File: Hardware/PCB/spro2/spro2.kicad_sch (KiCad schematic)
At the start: 7 parts

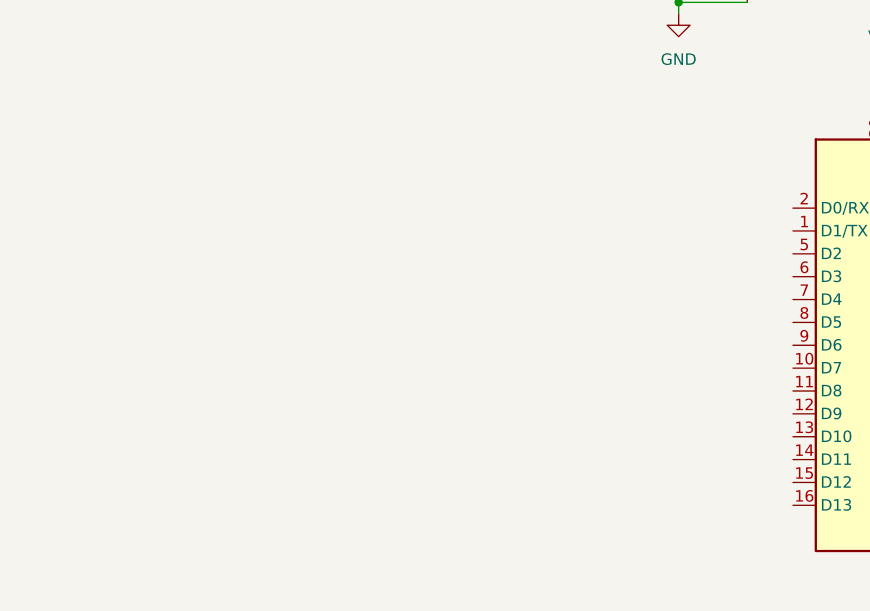
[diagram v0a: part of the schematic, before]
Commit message: Added the temperature schematics
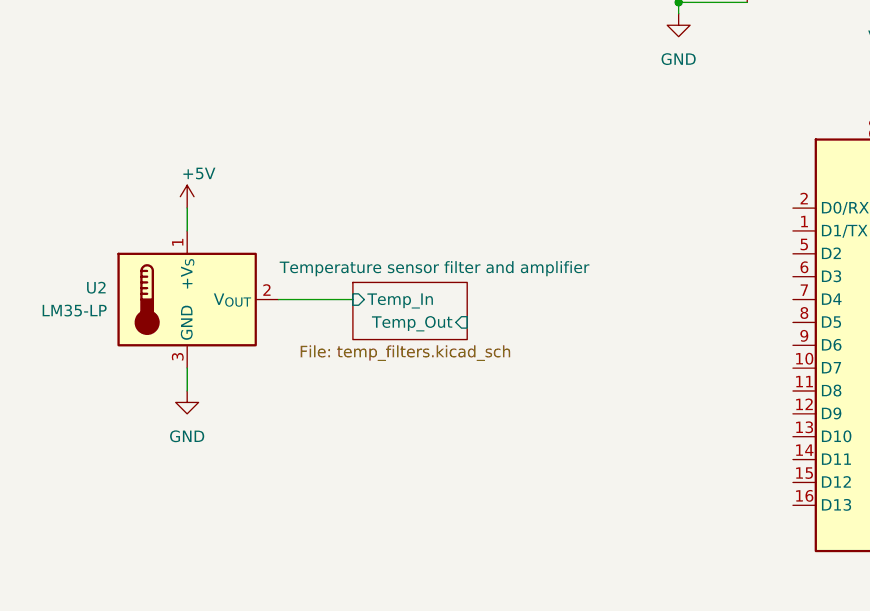
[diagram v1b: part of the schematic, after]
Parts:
- added U2: LM35-LP, Package_TO_SOT_THT:TO-92_Inline, symbol Sensor_Temperature:LM35-LP
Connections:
- net +5V: now also U2.1 (+V_{S})
- net GND: now also U2.3 (GND)
- new net Temperature sensor filter and amplifier/Temp_In: U2.2 (V_{OUT})
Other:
- added sheet Temperature sensor filter and amplifier (temp_filters.kicad_sch)

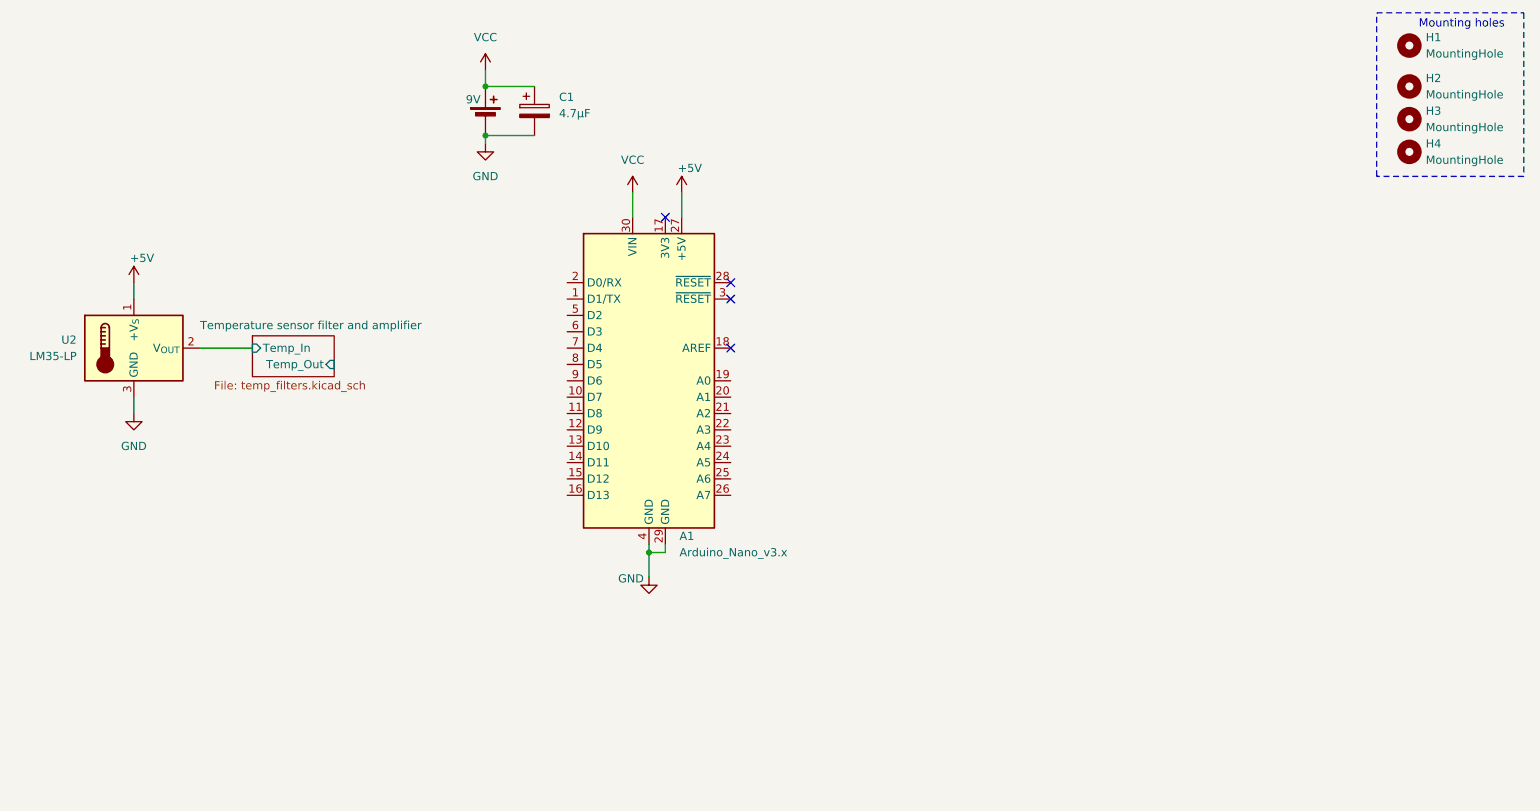
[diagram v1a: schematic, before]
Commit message: Updated circuit
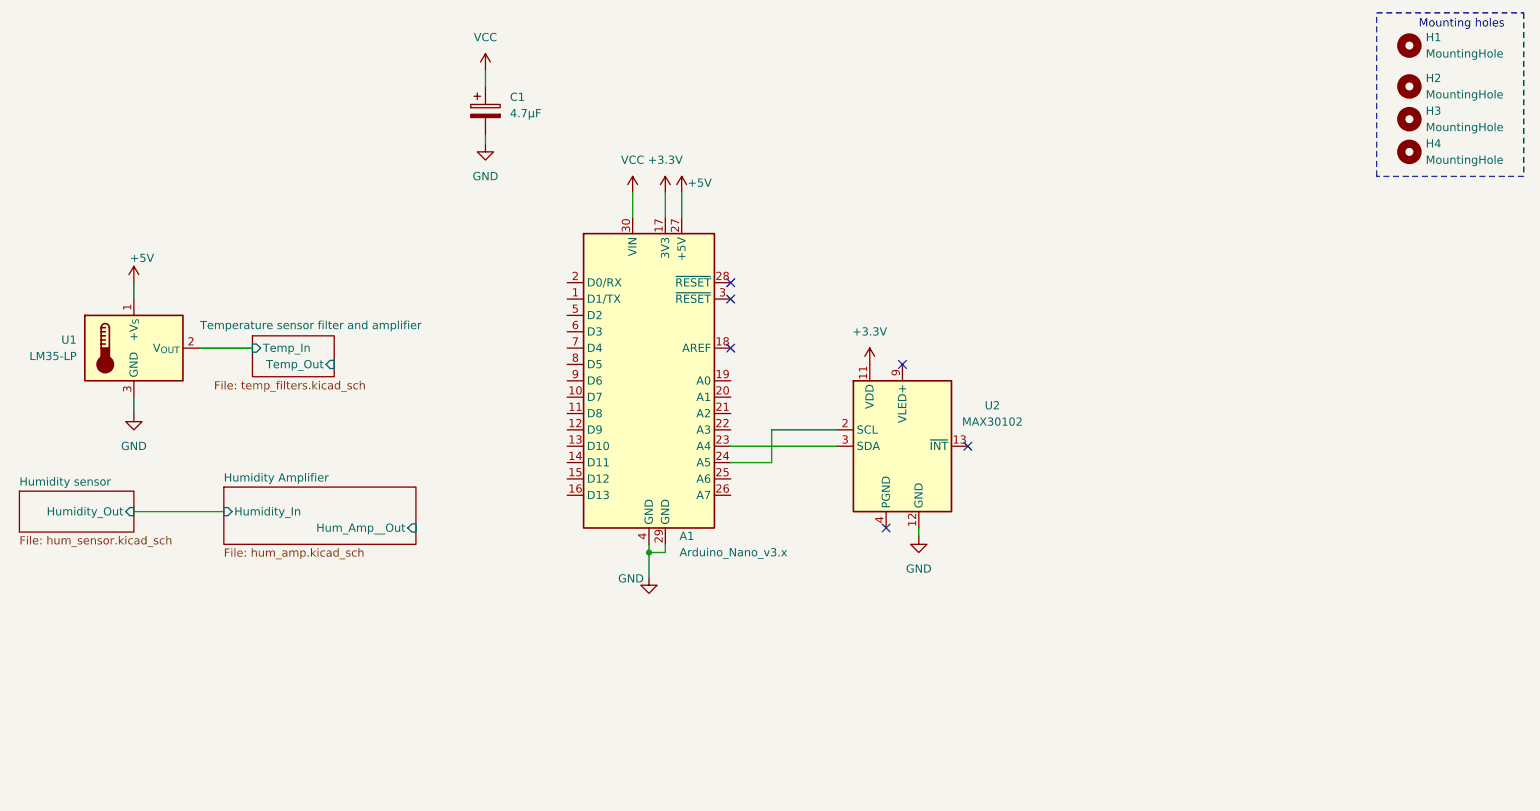
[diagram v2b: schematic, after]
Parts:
- removed BT1: 9V, Connector_PinHeader_2.54mm:PinHeader_1x02_P2.54mm_Vertical, symbol Device:Battery_Cell
- added U2: MAX30102, OptoDevice:Maxim_OLGA-14_3.3x5.6mm_P0.8mm, symbol Sensor:MAX30102
- renumbered U2 to U1
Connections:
- net GND: now also U2.12 (GND)
- net +3.3V: now reaches A1.17 (3V3)
- net +3.3V: now also U2.11 (VDD)
- net at A1.23 (A4): now also U2.3 (SDA)
- net at A1.24 (A5): now also U2.2 (SCL)
- new net: U2.10 (VLED+), U2.9 (VLED+)
- no-connect marks 4 -> 6
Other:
- added sheet Humidity Amplifier (hum_amp.kicad_sch)
- added sheet Humidity sensor (hum_sensor.kicad_sch)
- moved on the sheet: C1

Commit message: Updated schematic and 1st version of the PCB
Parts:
- removed U2: MAX30102, OptoDevice:Maxim_OLGA-14_3.3x5.6mm_P0.8mm, symbol Sensor:MAX30102
- added C6, C7, C9: 100n, Capacitor_THT:CP_Radial_D5.0mm_P2.00mm, symbol Device:C
- added C8: 4.7µF, Capacitor_THT:CP_Radial_D5.0mm_P2.00mm, symbol Device:C_Polarized
- added J2: MAX30102, Diplomna:connector_4p, symbol Connector:Screw_Terminal_01x04
- C1: footprint Library:CAPPRD200W45D500H500 -> Capacitor_THT:CP_Radial_D5.0mm_P2.00mm
- U1: footprint Package_TO_SOT_THT:TO-92_Inline -> Diplomna:connector_3p
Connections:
- net +3.3V: now also C8.1, C9.1, J2.3 (Pin_3)
- net +5V: now also C1.1, C6.1, C7.1
- net GND: now also C6.2, C7.2, C8.2, C9.2, J2.4 (Pin_4)
- net Temp: now reaches A1.19 (A0)
- net Humidity: now reaches A1.20 (A1)
- net at A1.23 (A4): now also J2.1 (Pin_1)
- net at A1.24 (A5): now also J2.2 (Pin_2)
- net VCC: no longer names the net of A1.30 (VIN)
- net VCC: no longer C1.1
- no-connect marks 6 -> 3
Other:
- moved on the sheet: C1

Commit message: Hopefully last version of PCB
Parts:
- C1: renamed from C9; footprint Capacitor_THT:CP_Radial_D5.0mm_P2.00mm -> Capacitor_THT:C_Rect_L7.2mm_W2.5mm_P5.00mm_FKS2_FKP2_MKS2_MKP2
- C3: renamed from C6; footprint Capacitor_THT:CP_Radial_D5.0mm_P2.00mm -> Capacitor_THT:C_Rect_L7.2mm_W2.5mm_P5.00mm_FKS2_FKP2_MKS2_MKP2
- C4: renamed from C7; footprint Capacitor_THT:CP_Radial_D5.0mm_P2.00mm -> Capacitor_THT:C_Rect_L7.2mm_W2.5mm_P5.00mm_FKS2_FKP2_MKS2_MKP2
- renumbered C8 to C2, C1 to C5, J2 to J1
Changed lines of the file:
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@@
 		(on_board yes)
 		(dnp no)
-		(property "Reference" "#PWR010"
+		(property "Reference" "#PWR011"
 			(at 175.26 97.79 0)
 			(effects
@@
 			(project "spro2"
 				(path "/edfea366-2226-45cc-893f-1155e0ffe333"
-					(reference "#PWR010")
+					(reference "#PWR011")
 					(unit 1)
 				)
@@
 		(on_board yes)
 		(dnp no)
-		(property "Reference" "#PWR08"
+		(property "Reference" "#PWR09"
 			(at 152.4 45.72 0)
 			(effects
@@
 			(project "spro2"
 				(path "/edfea366-2226-45cc-893f-1155e0ffe333"
-					(reference "#PWR08")
+					(reference "#PWR09")
 					(unit 1)
 				)
@@
 		(on_board yes)
 		(dnp no)
-		(property "Reference" "#PWR027"
+		(property "Reference" "#PWR05"
 			(at 115.57 118.11 0)
 			(effects
@@
 			(project "spro2"
 				(path "/edfea366-2226-45cc-893f-1155e0ffe333"
-					(reference "#PWR027")
+					(reference "#PWR05")
 					(unit 1)
 				)
@@
 		(on_board yes)
 		(dnp no)
-		(property "Reference" "C7"
+		(property "Reference" "C4"
 			(at 118.872 120.65 0)
 			(effects
@@
 			)
 		)
-		(property "Footprint" "Capacitor_THT:CP_Radial_D5.0mm_P2.00mm"
+		(property "Footprint" "Capacitor_THT:C_Rect_L7.2mm_W2.5mm_P5.00mm_FKS2_FKP2_MKS2_MKP2"
 			(at 116.5352 125.73 0)
 			(effects
@@
 			(project "spro2"
 				(path "/edfea366-2226-45cc-893f-1155e0ffe333"
-					(reference "C7")
+					(reference "C4")
 					(unit 1)
 				)
@@
 		(on_board yes)
 		(dnp no)
-		(property "Reference" "C6"
+		(property "Reference" "C3"
 			(at 107.442 120.65 0)
 			(effects
@@
 			)
 		)
-		(property "Footprint" "Capacitor_THT:CP_Radial_D5.0mm_P2.00mm"
+		(property "Footprint" "Capacitor_THT:C_Rect_L7.2mm_W2.5mm_P5.00mm_FKS2_FKP2_MKS2_MKP2"
 			(at 105.1052 125.73 0)
 			(effects
@@
 			(project "spro2"
 				(path "/edfea366-2226-45cc-893f-1155e0ffe333"
-					(reference "C6")
+					(reference "C3")
 					(unit 1)
 				)
@@
 		(dnp no)
 		(fields_autoplaced yes)
-		(property "Reference" "#PWR030"
+		(property "Reference" "#PWR04"
 			(at 81.28 134.62 0)
 			(effects
@@
 			(project "spro2"
 				(path "/edfea366-2226-45cc-893f-1155e0ffe333"
-					(reference "#PWR030")
+					(reference "#PWR04")
 					(unit 1)
 				)
@@
 		(dnp no)
 		(fields_autoplaced yes)
-		(property "Reference" "J2"
+		(property "Reference" "J1"
 			(at 184.15 83.8199 0)
 			(effects
@@
 			(project ""
 				(path "/edfea366-2226-45cc-893f-1155e0ffe333"
-					(reference "J2")
+					(reference "J1")
 					(unit 1)
 				)
@@
 		(dnp no)
 		(fields_autoplaced yes)
-		(property "Reference" "C1"
+		(property "Reference" "C5"
 			(at 130.81 119.7609 0)
 			(effects
@@
 			(project "spro2"
 				(path "/edfea366-2226-45cc-893f-1155e0ffe333"
-					(reference "C1")
+					(reference "C5")
 					(unit 1)
 				)
@@
 		(dnp no)
 		(fields_autoplaced yes)
-		(property "Reference" "C8"
+		(property "Reference" "C2"
 			(at 91.44 119.7609 0)
 			(effects
@@
 			(project "spro2"
 				(path "/edfea366-2226-45cc-893f-1155e0ffe333"
-					(reference "C8")
+					(reference "C2")
 					(unit 1)
 				)
@@
 		(on_board yes)
 		(dnp no)
-		(property "Reference" "#PWR09"
+		(property "Reference" "#PWR010"
 			(at 175.26 80.01 0)
 			(effects
@@
 			(project "spro2"
 				(path "/edfea366-2226-45cc-893f-1155e0ffe333"
-					(reference "#PWR09")
+					(reference "#PWR010")
 					(unit 1)
 				)
@@
 		(dnp no)
 		(fields_autoplaced yes)
-		(property "Reference" "#PWR029"
+		(property "Reference" "#PWR03"
 			(at 81.28 119.38 0)
 			(effects
@@
 			(project "spro2"
 				(path "/edfea366-2226-45cc-893f-1155e0ffe333"
-					(reference "#PWR029")
+					(reference "#PWR03")
 					(unit 1)
 				)
@@
 		(on_board yes)
 		(dnp no)
-		(property "Reference" "C9"
+		(property "Reference" "C1"
 			(at 78.232 120.65 0)
 			(effects
@@
 			)
 		)
-		(property "Footprint" "Capacitor_THT:CP_Radial_D5.0mm_P2.00mm"
+		(property "Footprint" "Capacitor_THT:C_Rect_L7.2mm_W2.5mm_P5.00mm_FKS2_FKP2_MKS2_MKP2"
 			(at 75.8952 125.73 0)
 			(effects
@@
 			(project "spro2"
 				(path "/edfea366-2226-45cc-893f-1155e0ffe333"
-					(reference "C9")
+					(reference "C1")
 					(unit 1)
 				)
@@
 		(dnp no)
 		(fields_autoplaced yes)
-		(property "Reference" "#PWR07"
+		(property "Reference" "#PWR08"
 			(at 149.86 45.72 0)
 			(effects
@@
 			(project ""
 				(path "/edfea366-2226-45cc-893f-1155e0ffe333"
-					(reference "#PWR07")
+					(reference "#PWR08")
 					(unit 1)
 				)
@@
 		(dnp no)
 		(fields_autoplaced yes)
-		(property "Reference" "#PWR028"
+		(property "Reference" "#PWR06"
 			(at 115.57 135.89 0)
 			(effects
@@
 			(project "spro2"
 				(path "/edfea366-2226-45cc-893f-1155e0ffe333"
-					(reference "#PWR028")
+					(reference "#PWR06")
 					(unit 1)
 				)
@@
 		(on_board yes)
 		(dnp no)
-		(property "Reference" "#PWR06"
+		(property "Reference" "#PWR07"
 			(at 147.32 107.95 0)
 			(effects
@@
 			(project "spro2"
 				(path "/edfea366-2226-45cc-893f-1155e0ffe333"
-					(reference "#PWR06")
-					(unit 1)
-				)
+					(reference "#PWR07")
+					(unit 1)
+				)

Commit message: pcb finalized
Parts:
- C2, C5: footprint Capacitor_THT:CP_Radial_D5.0mm_P2.00mm -> Capacitor_THT:CP_Radial_D7.5mm_P2.50mm
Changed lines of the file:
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@@
 (kicad_sch
-	(version 20231120)
+	(version 20250114)
 	(generator "eeschema")
-	(generator_version "8.0")
+	(generator_version "9.0")
 	(paper "A4")
 	(title_block
@@
 		(company "Group 3")
 	)
+	(rectangle
+		(start 283.21 74.93)
+		(end 283.21 74.93)
+		(stroke
+			(width 0)
+			(type default)
+		)
+		(fill
+			(type none)
+		)
+	)
+	(text "Mounting holes"
+		(exclude_from_sim no)
+		(at 273.558 15.748 0)
+		(effects
+			(font
+				(size 1.27 1.27)
+			)
+		)
+	)
+	(text_box ""
+		(exclude_from_sim no)
+		(at 260.35 13.97 0)
+		(size 22.86 25.4)
+		(margins 0.9525 0.9525 0.9525 0.9525)
+		(stroke
+			(width 0)
+			(type dash_dot_dot)
+		)
+		(fill
+			(type none)
+		)
+		(effects
+			(font
+				(size 1.27 1.27)
+			)
+			(justify left top)
+		)
+	)
 	(junction
 		(at 115.57 128.27)
@@
 		)
 	)
-	(rectangle
-		(start 283.21 74.93)
-		(end 283.21 74.93)
-		(stroke
-			(width 0)
-			(type default)
-		)
-		(fill
-			(type none)
-		)
-	)
-	(text_box ""
-		(exclude_from_sim no)
-		(at 260.35 13.97 0)
-		(size 22.86 25.4)
-		(stroke
-			(width 0)
-			(type dash_dot_dot)
-		)
-		(fill
-			(type none)
-		)
+	(label "Humidity"
+		(at 162.56 73.66 0)
 		(effects
 			(font
 				(size 1.27 1.27)
 			)
-			(justify left top)
-		)
-	)
-	(text "Mounting holes"
-		(exclude_from_sim no)
-		(at 273.558 15.748 0)
+			(justify left bottom)
+		)
+	)
+	(label "Temp"
+		(at 162.56 71.12 0)
 		(effects
 			(font
 				(size 1.27 1.27)
 			)
-		)
-	)
-	(label "Humidity"
-		(at 162.56 73.66 0)
-		(fields_autoplaced yes)
+			(justify left bottom)
+		)
+	)
+	(label "Temp"
+		(at 106.68 68.58 0)
 		(effects
 			(font
@@
 		)
 	)
-	(label "Temp"
-		(at 162.56 71.12 0)
-		(fields_autoplaced yes)
-		(effects
-			(font
-				(size 1.27 1.27)
-			)
-			(justify left bottom)
-		)
-	)
-	(label "Temp"
-		(at 106.68 68.58 0)
-		(fields_autoplaced yes)
-		(effects
-			(font
-				(size 1.27 1.27)
-			)
-			(justify left bottom)
-		)
-	)
 	(label "Humidity"
 		(at 116.84 93.98 0)
-		(fields_autoplaced yes)
 		(effects
 			(font
@@
 			)
 		)
-		(property "Footprint" "Capacitor_THT:CP_Radial_D5.0mm_P2.00mm"
+		(property "Footprint" "Capacitor_THT:CP_Radial_D7.5mm_P2.50mm"
 			(at 127.9652 125.73 0)
 			(effects
@@
 			)
 		)
-		(property "Footprint" "Capacitor_THT:CP_Radial_D5.0mm_P2.00mm"
+		(property "Footprint" "Capacitor_THT:CP_Radial_D7.5mm_P2.50mm"
 			(at 88.5952 125.73 0)
 			(effects
@@
 		(at 87.63 64.135)
 		(size 12.7 6.35)
+		(exclude_from_sim no)
+		(in_bom yes)
+		(on_board yes)
+		(dnp no)
 		(stroke
 			(width 0.1524)
@@
 		(at 49.53 88.265)
 		(size 17.78 6.35)
+		(exclude_from_sim no)
+		(in_bom yes)
+		(on_board yes)
+		(dnp no)
 		(fields_autoplaced yes)
 		(stroke
@@
 		(at 83.185 87.63)
 		(size 29.845 8.89)
+		(exclude_from_sim no)
+		(in_bom yes)
+		(on_board yes)
+		(dnp no)
 		(fields_autoplaced yes)
 		(stroke
@@
 		)
 	)
+	(embedded_fonts no)
 )

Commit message: Finished PCB
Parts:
- J1: footprint Diplomna:connector_4p -> SPRO_lib:connector_4p
- U1: footprint Diplomna:connector_3p -> SPRO_lib:connector_3p
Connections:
- no-connect marks 3 -> 22
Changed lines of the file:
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@@
+	)
+	(no_connect
+		(at 134.62 86.36)
+	)
+	(no_connect
+		(at 134.62 83.82)
+	)
+	(no_connect
+		(at 134.62 60.96)
 	)
 	(no_connect
@@
 	)
 	(no_connect
+		(at 160.02 76.2)
+	)
+	(no_connect
+		(at 160.02 86.36)
+	)
+	(no_connect
+		(at 134.62 58.42)
+	)
+	(no_connect
+		(at 134.62 81.28)
+	)
+	(no_connect
+		(at 144.78 45.72)
+	)
+	(no_connect
+		(at 134.62 68.58)
+	)
+	(no_connect
+		(at 134.62 55.88)
+	)
+	(no_connect
+		(at 134.62 78.74)
+	)
+	(no_connect
+		(at 160.02 78.74)
+	)
+	(no_connect
+		(at 134.62 66.04)
+	)
+	(no_connect
+		(at 134.62 73.66)
+	)
+	(no_connect
+		(at 134.62 76.2)
+	)
+	(no_connect
+		(at 134.62 71.12)
+	)
+	(no_connect
 		(at 160.02 66.04)
 	)
 	(no_connect
+		(at 134.62 88.9)
+	)
+	(no_connect
 		(at 160.02 58.42)
+	)
+	(no_connect
+		(at 134.62 63.5)
+	)
+	(no_connect
+		(at 160.02 88.9)
 	)
 	(wire
@@
 			)
 		)
-		(property "Footprint" "Diplomna:connector_4p"
+		(property "Footprint" "SPRO_lib:connector_4p"
 			(at 181.61 83.82 0)
 			(effects
@@
 			)
 		)
-		(property "Footprint" "Diplomna:connector_3p"
+		(property "Footprint" "SPRO_lib:connector_3p"
 			(at 68.58 72.39 0)
 			(effects

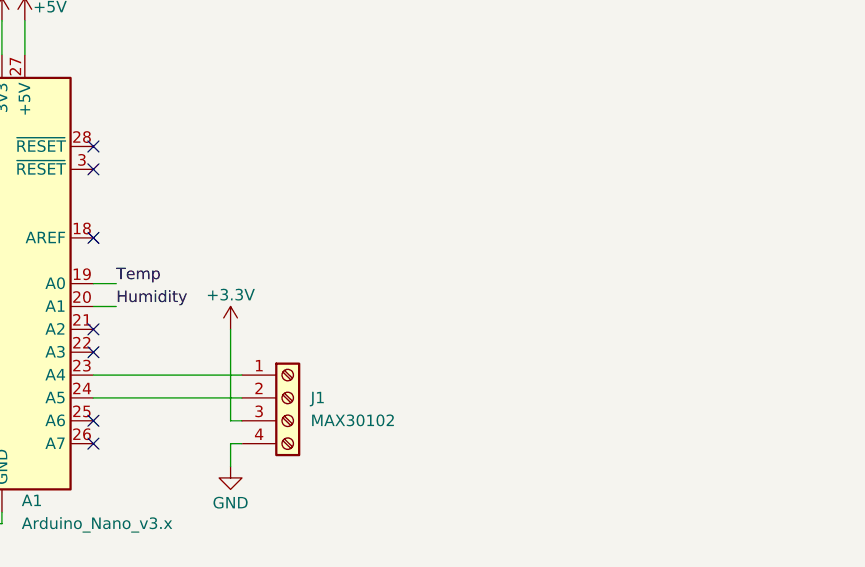
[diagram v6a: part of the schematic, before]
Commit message: Added the LCD to schematic
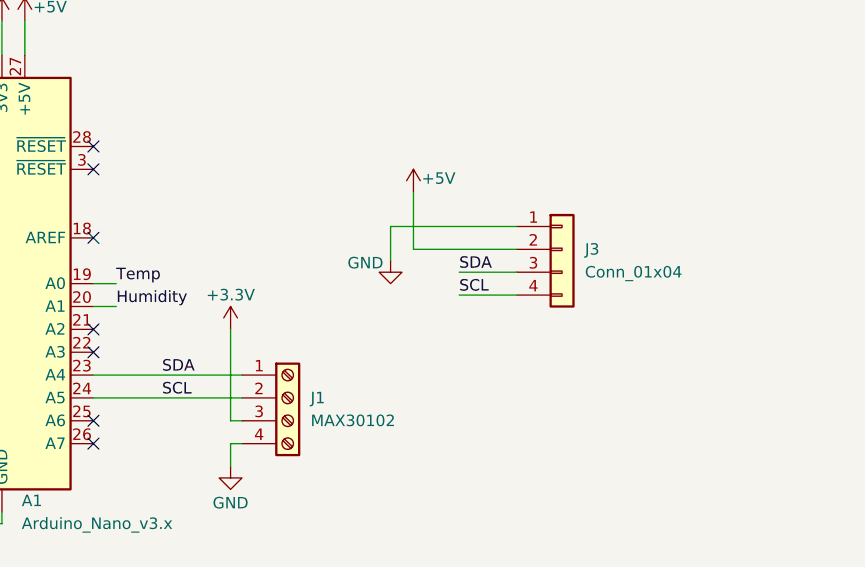
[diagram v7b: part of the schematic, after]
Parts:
- added J3: Conn_01x04, symbol Connector_Generic:Conn_01x04
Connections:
- net +5V: now also J3.2 (Pin_2)
- net GND: now also J3.1 (Pin_1)
- net SDA: now reaches A1.23 (A4), J1.1 (Pin_1)
- net SDA: now also J3.3 (Pin_3)
- net SCL: now reaches A1.24 (A5), J1.2 (Pin_2)
- net SCL: now also J3.4 (Pin_4)
